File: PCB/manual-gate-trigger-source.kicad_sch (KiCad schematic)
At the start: 27 parts

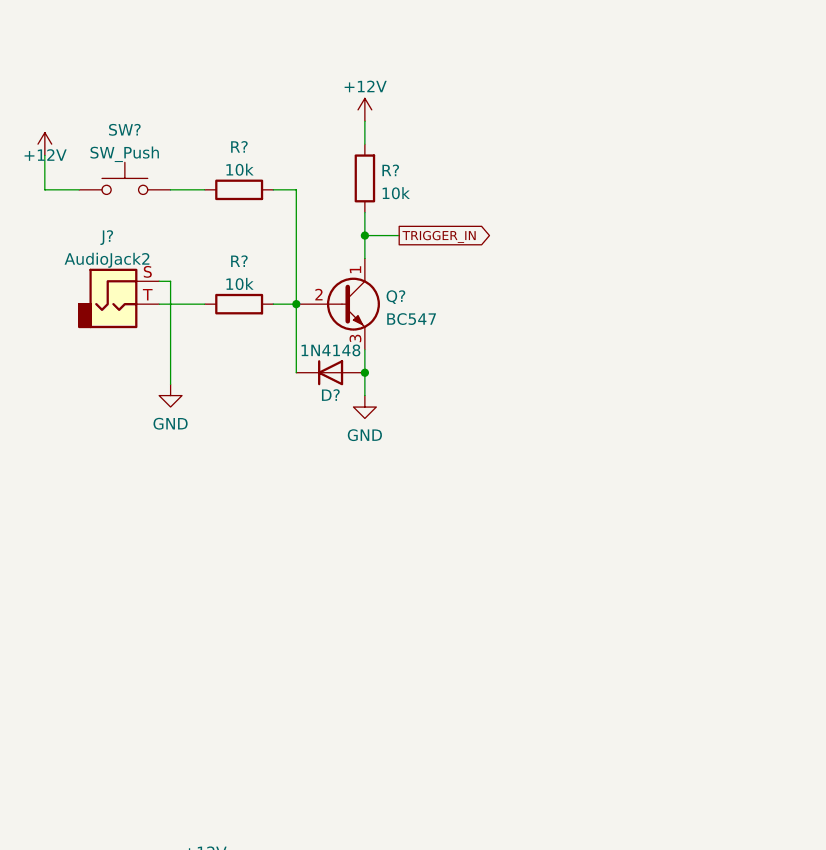
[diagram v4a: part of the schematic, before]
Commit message: :art: Debounce the trigger button
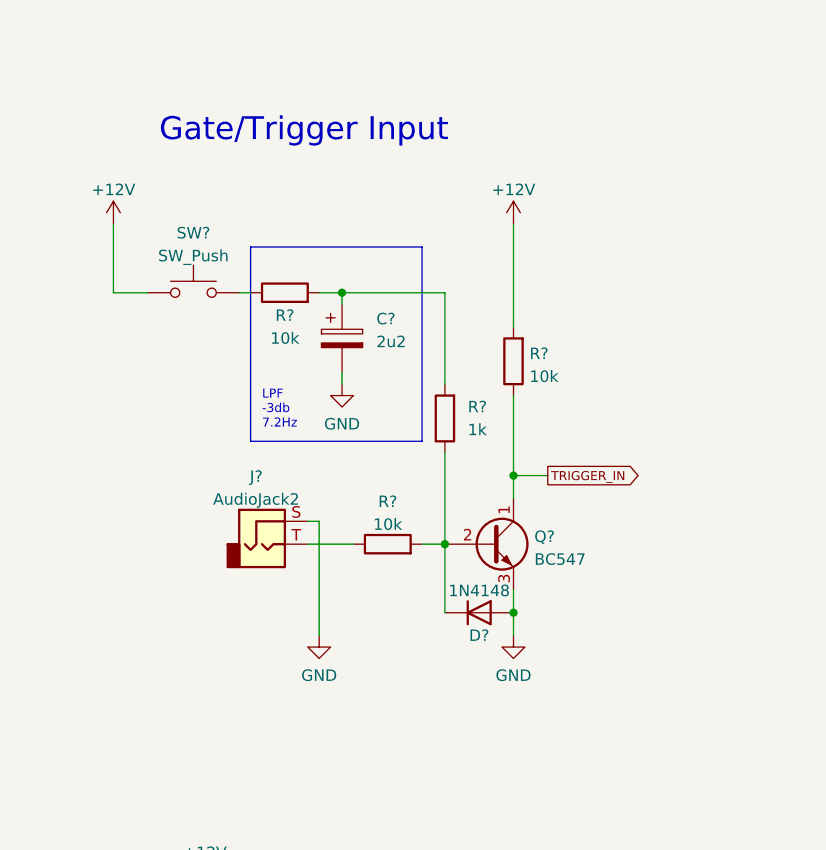
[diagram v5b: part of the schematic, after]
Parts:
- added C?: 2u2, symbol Device:C_Polarized
- added R?: 1k, symbol Device:R
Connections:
- net GND: now also C?.2
- net at D?.1 (K), Q?.2 (B), R?.2: now also R?.1; no longer R?.2
- new net: C?.1, R?.2, R?.2
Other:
- note added: "Gate/Trigger Input"
- moved on the sheet: D?, J?, Q?, R?, SW?

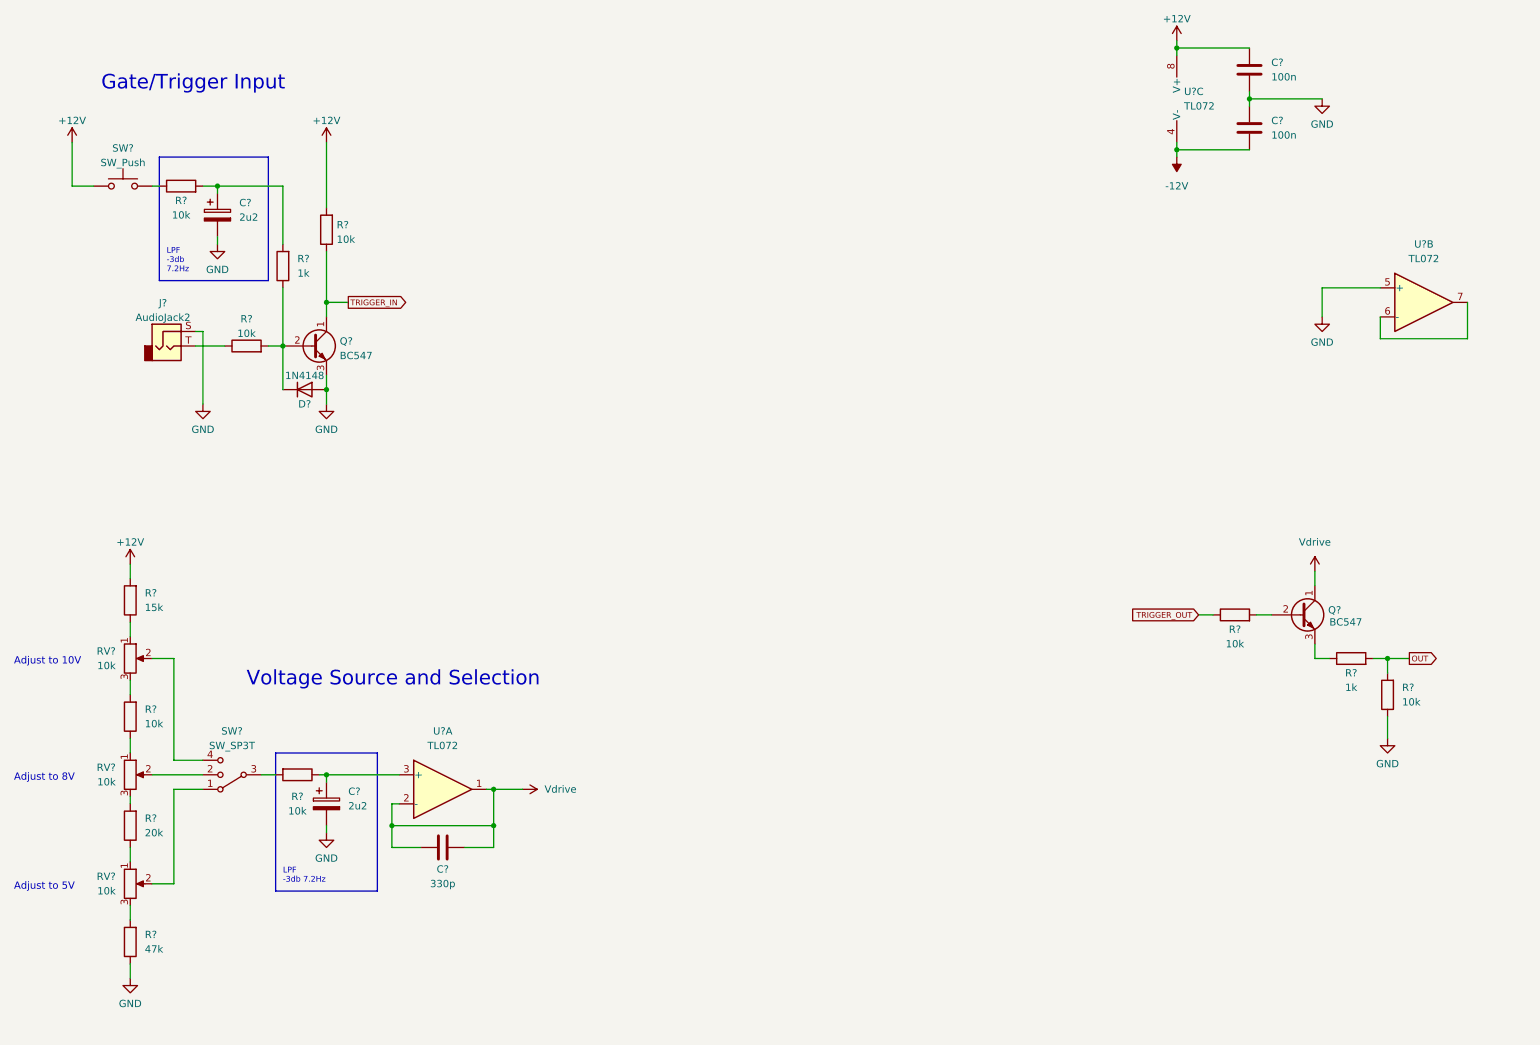
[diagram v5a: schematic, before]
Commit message: :sparkles: Add control for minimum gate and trigger length
https://www.elektronik-kompendium.de/sites/slt/0310121.htm?mr=100330&mc=10u&mth=2%2C42798
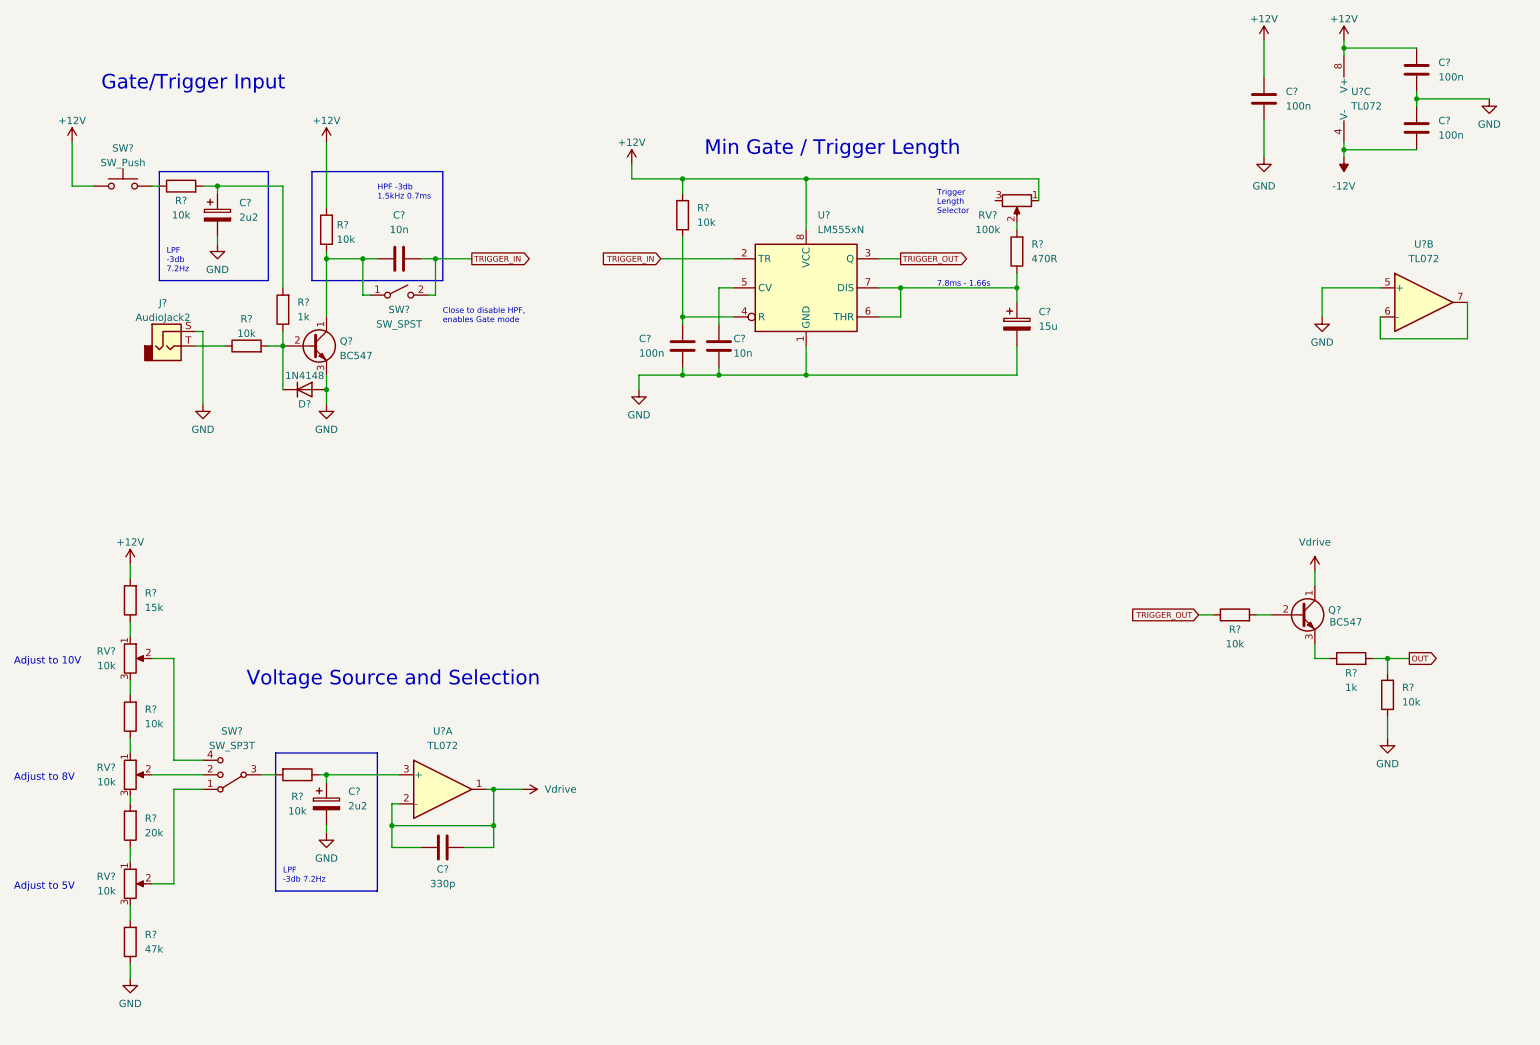
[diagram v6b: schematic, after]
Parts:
- added C? (x2): 100n, symbol Device:C
- added C? (x2): 10n, symbol Device:C
- added C?: 15u, symbol Device:C_Polarized
- added R?: 10k, symbol Device:R
- added R?: 470R, symbol Device:R
- added RV?: 100k, symbol Device:R_Potentiometer
- added SW?: SW_SPST, symbol Switch:SW_SPST
- added U?: LM555xN, Package_DIP:DIP-8_W7.62mm, symbol Timer:LM555xN
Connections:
- net +12V: now also C?.1, R?.2, RV?.1, U?.8 (VCC)
- net GND: now also C?.2, C?.2, C?.2, C?.2, U?.1 (GND)
- net TRIGGER_IN: now also C?.2, SW?.2 (B), U?.2 (TR); no longer Q?.1 (C), R?.1
- net TRIGGER_OUT: now also U?.3 (Q)
- new net: C?.1, R?.1, U?.4 (R)
- new net: C?.1, Q?.1 (C), R?.1, SW?.1 (A)
- new net: C?.1, U?.5 (CV)
- new net: C?.1, R?.1, U?.6 (THR), U?.7 (DIS)
- new net: R?.2, RV?.2
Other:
- note added: "7.8ms - 1.66s"
- note added: "Close to disable HPF, enables Gate mode"
- note added: "HPF -3db 1.5kHz 0.7ms"
- note added: "Min Gate / Trigger Length"
- note added: "Trigger Length Selector"
- moved on the sheet: C?, R?, U?C

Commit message: :sparkles: Sort out gate/trigger output
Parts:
- added D?: rt, symbol Device:LED
- added J?: Out 2, symbol Connector:AudioJack2
- added J?: Out 1, symbol Connector:AudioJack2
- added R?: 470R, symbol Device:R
- added R?: 1k, symbol Device:R
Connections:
- net GND: now also D?.1 (K), J?.S, J?.S
- net TRIGGER_OUT: now also R?.2
- net at Q?.3 (E), R?.1: now also R?.2, R?.1
- net OUT: no longer names the net of R?.2
- net OUT: now also J?.T; no longer R?.2
- new net: D?.2 (A), R?.1
- new net: J?.T, R?.2
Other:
- note added: "Gate/Trigger Output"
- moved on the sheet: C?, Q?, R?, U?B, U?C

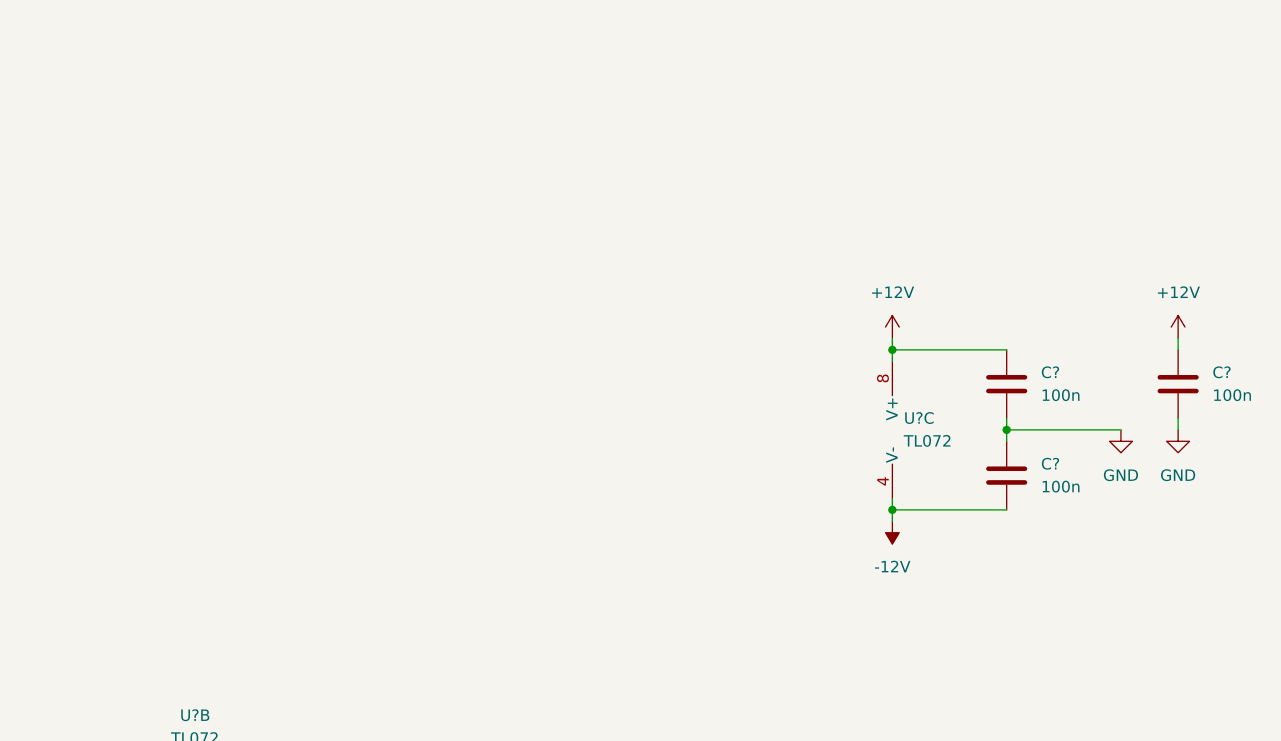
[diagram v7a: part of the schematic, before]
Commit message: :sparkles: Set up power supply and filtering
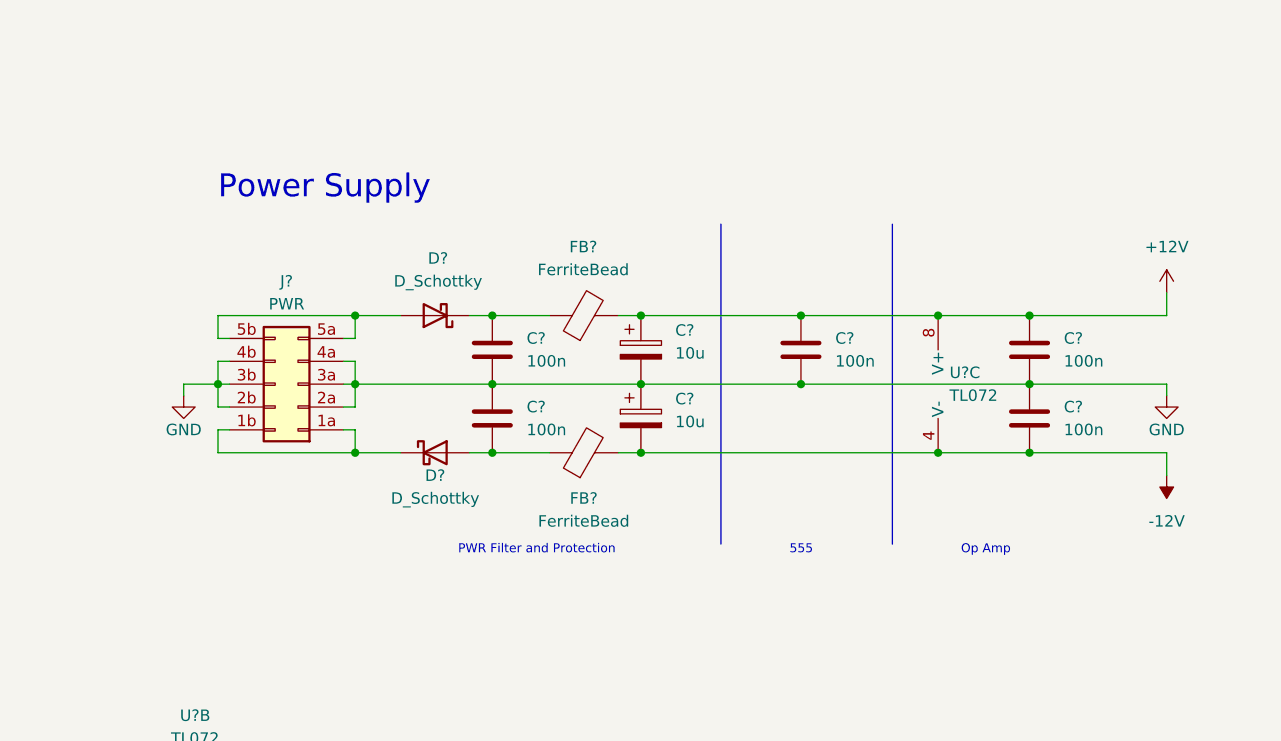
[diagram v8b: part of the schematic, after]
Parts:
- added C? (x2): 100n, symbol Device:C
- added C? (x2): 10u, symbol Device:C_Polarized
- added D? (x2): D_Schottky, symbol Device:D_Schottky
- added FB? (x2): FerriteBead, symbol Device:FerriteBead
- added J?: PWR, symbol Connector_Generic:Conn_02x05_Row_Letter_Last
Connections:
- net +12V: now also C?.1, FB?.2
- net -12V: now also C?.2, FB?.2
- net GND: now also C?.1, C?.1, C?.2, C?.2, J?.2a (Pin_2a), J?.2b (Pin_2b), J?.3a (Pin_3a), J?.3b (Pin_3b), J?.4a (Pin_4a), J?.4b (Pin_4b)
- new net: C?.2, D?.2 (A), FB?.1
- new net: C?.1, D?.1 (K), FB?.1
- new net: D?.1 (K), J?.1a (Pin_1a), J?.1b (Pin_1b)
- new net: D?.2 (A), J?.5a (Pin_5a), J?.5b (Pin_5b)
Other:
- note added: "555"
- note added: "Op Amp"
- note added: "PWR Filter and Protection"
- note added: "Power Supply"
- moved on the sheet: C?, U?C
